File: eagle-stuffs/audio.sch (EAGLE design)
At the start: 35 parts, among them IC1 SSM2211SZ, IC2 TL084P, IC3 DS1804-100k, IC4 DS1804-10k

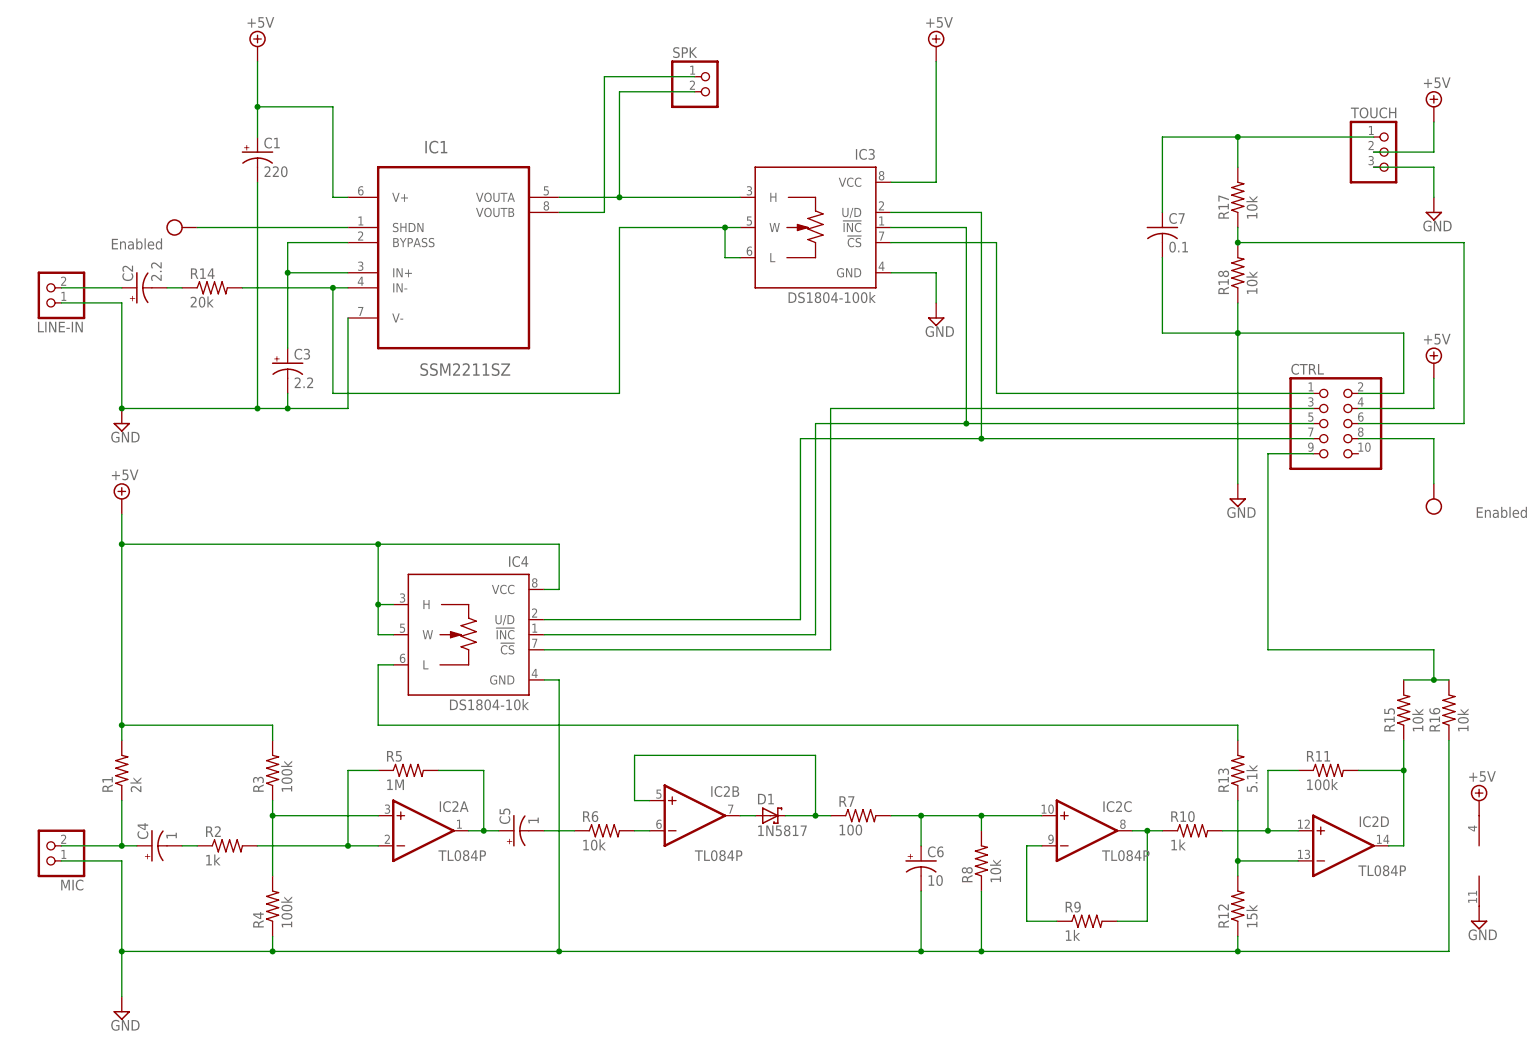
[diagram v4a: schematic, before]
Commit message: Removed second digital pot
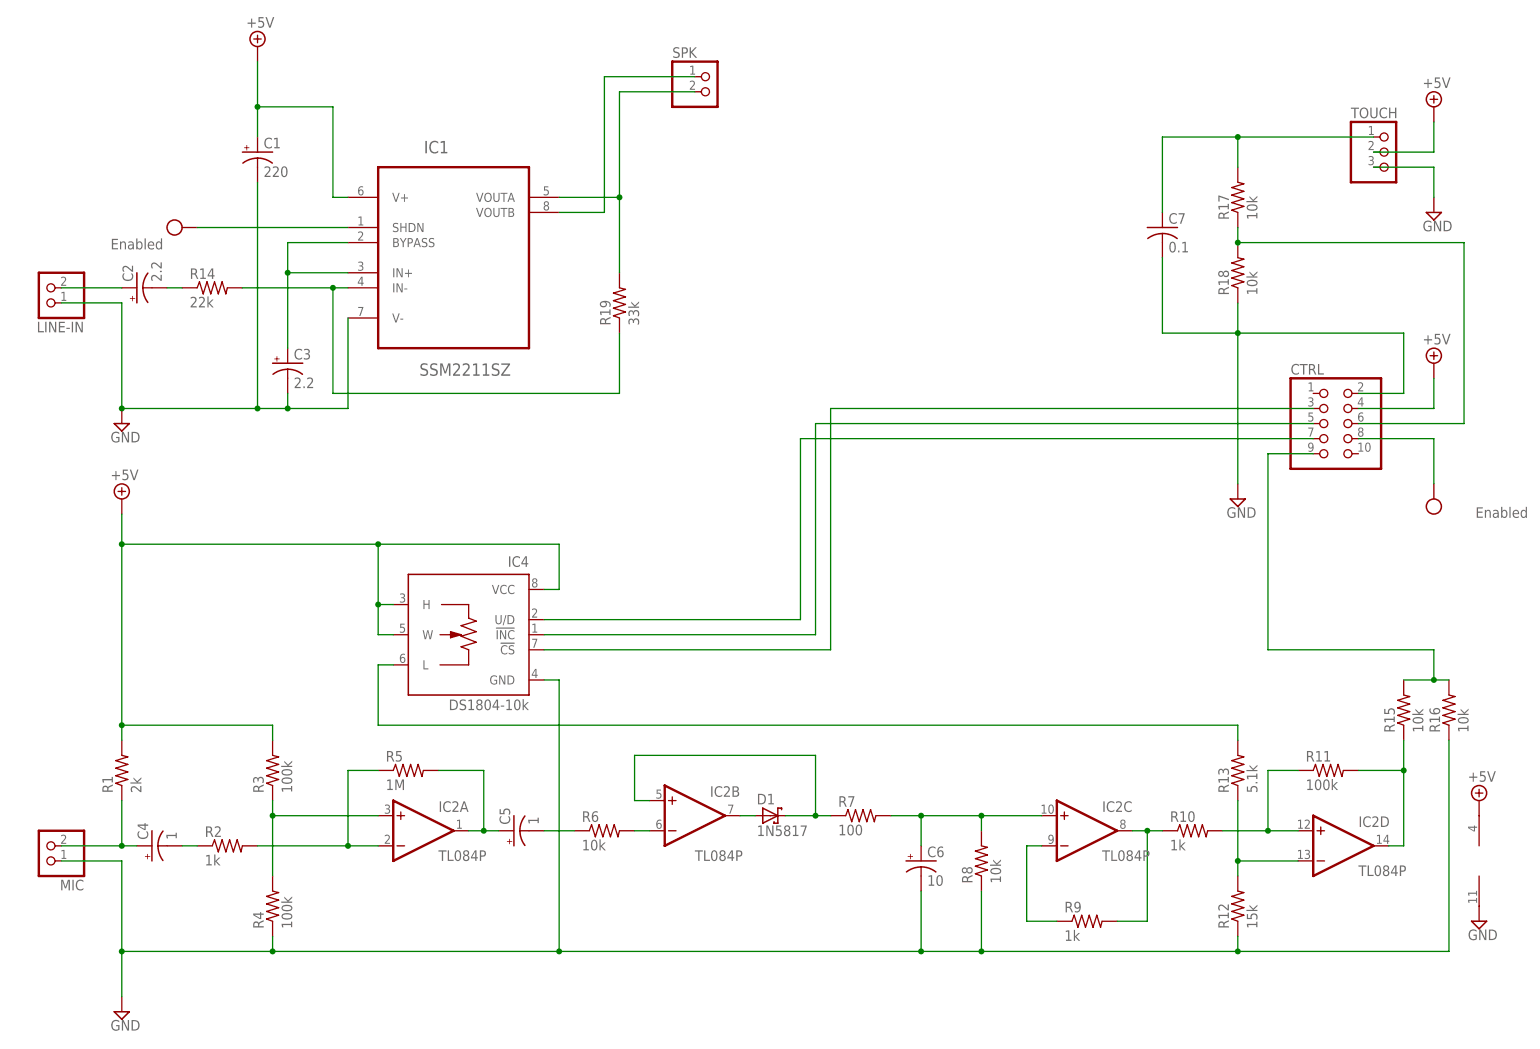
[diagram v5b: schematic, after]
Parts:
- removed IC3: DS1804-100k, pot-xicor:X9C102P
- added R19: 33k, rcl:R-US_0204/2V
- R14: value 20k -> 22k
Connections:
- removed net N$18: CTRL.1, IC3.!CS
- net +5V: no longer IC3.VCC
- net GND: no longer IC3.GND
- net N$1: now also R19.2; no longer IC3.H
- net N$20: no longer IC3.!INC
- net N$21: no longer IC3.U/D
- net N$4: now also R19.1; no longer IC3.L, IC3.W
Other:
- note added: "C"
- note removed: "B"
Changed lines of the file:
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@@
 <part name="FRAME1" library="frames" deviceset="FRAME_A_L" device=""/>
 <part name="IC2" library="linear" deviceset="TL084" device="P"/>
-<part name="IC3" library="pot-xicor" deviceset="X9C102*" device="P" value="DS1804-100k"/>
 <part name="IC4" library="pot-xicor" deviceset="X9C102*" device="P" value="DS1804-10k"/>
 <part name="SUPPLY1" library="supply2" deviceset="+5V" device=""/>
@@
 <part name="SUPPLY3" library="supply2" deviceset="VCC" device="" value="Enabled"/>
 <part name="SUPPLY6" library="supply2" deviceset="VCC" device="" value="Enabled"/>
-<part name="SUPPLY9" library="supply2" deviceset="+5V" device=""/>
-<part name="SUPPLY14" library="supply2" deviceset="GND" device=""/>
 <part name="TOUCH" library="adafruit" deviceset="PINHD-1X3" device=""/>
 <part name="SUPPLY15" library="supply2" deviceset="+5V" device=""/>
@@
 <part name="D1" library="adafruit" deviceset="SCHOTTKY-DIODE" device="DO41-7" value="1N5817"/>
 <part name="C6" library="rcl" deviceset="CPOL-US" device="E2-4" value="10"/>
-<part name="R14" library="rcl" deviceset="R-US_" device="0204/2V" value="20k"/>
+<part name="R14" library="rcl" deviceset="R-US_" device="0204/2V" value="22k"/>
 <part name="R2" library="rcl" deviceset="R-US_" device="0204/2V" value="1k"/>
 <part name="R5" library="rcl" deviceset="R-US_" device="0204/2V" value="1M"/>
@@
 <part name="R18" library="rcl" deviceset="R-US_" device="0204/2V" value="10k"/>
 <part name="C7" library="rcl" deviceset="C-US" device="025-024X044" value="0.1"/>
+<part name="R19" library="rcl" deviceset="R-US_" device="0204/2V" value="33k"/>
 </parts>
 <sheets>
@@
 <text x="193.04" y="25.4" size="2.54" layer="98" font="fixed">Y.A.N.C. (Yet Another Nixie Clock)</text>
 <text x="175.26" y="7.62" size="2.54" layer="98" font="fixed">Licensed under CERN OHL v.1.2 or later</text>
-<text x="264.16" y="7.62" size="2.54" layer="98" font="fixed">B</text>
+<text x="264.16" y="7.62" size="2.54" layer="98" font="fixed">C</text>
 <text x="76.2" y="45.72" size="1.778" layer="98" font="fixed">Preamp</text>
 <text x="132.08" y="45.72" size="1.778" layer="98" font="fixed">Envelope follower</text>
@@
 <attribute name="VALUE" x="129.54" y="66.04" size="1.778" layer="96"/>
 </instance>
-<instance part="IC3" gate="1" x="149.86" y="172.72" rot="MR0"/>
 <instance part="IC4" gate="1" x="91.44" y="104.14" rot="MR0"/>
 <instance part="SUPPLY1" gate="+5V" x="254" y="149.86"/>
@@
 <attribute name="VALUE" x="269.875" y="123.825" size="1.778" layer="96" rot="MR0"/>
 </instance>
-<instance part="SUPPLY9" gate="+5V" x="170.18" y="203.2" smashed="yes">
-<attribute name="VALUE" x="168.275" y="206.375" size="1.778" layer="96"/>
-</instance>
-<instance part="SUPPLY14" gate="GND" x="170.18" y="157.48"/>
 <instance part="TOUCH" gate="A" x="246.38" y="185.42"/>
 <instance part="SUPPLY15" gate="+5V" x="254" y="193.04"/>
@@
 <instance part="R18" gate="G$1" x="220.98" y="165.1" rot="R90"/>
 <instance part="C7" gate="G$1" x="208.28" y="172.72"/>
+<instance part="R19" gate="G$1" x="116.84" y="160.02" rot="R90"/>
 </instances>
 <busses>
@@
 </segment>
 <segment>
-<pinref part="IC3" gate="1" pin="GND"/>
-<pinref part="SUPPLY14" gate="GND" pin="GND"/>
-<wire x1="162.56" y1="165.1" x2="170.18" y2="165.1" width="0.1524" layer="91"/>
-<wire x1="170.18" y1="165.1" x2="170.18" y2="160.02" width="0.1524" layer="91"/>
-</segment>
-<segment>
 <pinref part="TOUCH" gate="A" pin="3"/>
 <wire x1="243.84" y1="182.88" x2="254" y2="182.88" width="0.1524" layer="91"/>
@@
 </segment>
 <segment>
-<pinref part="IC3" gate="1" pin="VCC"/>
-<pinref part="SUPPLY9" gate="+5V" pin="+5V"/>
-<wire x1="162.56" y1="180.34" x2="170.18" y2="180.34" width="0.1524" layer="91"/>
-<wire x1="170.18" y1="180.34" x2="170.18" y2="200.66" width="0.1524" layer="91"/>
-</segment>
-<segment>
 <pinref part="TOUCH" gate="A" pin="2"/>
 <pinref part="SUPPLY15" gate="+5V" pin="+5V"/>
@@
 <segment>
 <pinref part="IC4" gate="1" pin="!INC"/>
-<wire x1="149.86" y1="139.7" x2="175.26" y2="139.7" width="0.1524" layer="91"/>
-<wire x1="175.26" y1="139.7" x2="233.68" y2="139.7" width="0.1524" layer="91"/>
+<wire x1="149.86" y1="139.7" x2="233.68" y2="139.7" width="0.1524" layer="91"/>
 <wire x1="104.14" y1="104.14" x2="149.86" y2="104.14" width="0.1524" layer="91"/>
 <wire x1="149.86" y1="104.14" x2="149.86" y2="139.7" width="0.1524" layer="91"/>
 <pinref part="CTRL" gate="A" pin="5"/>
-<pinref part="IC3" gate="1" pin="!INC"/>
-<wire x1="162.56" y1="172.72" x2="175.26" y2="172.72" width="0.1524" layer="91"/>
-<wire x1="175.26" y1="172.72" x2="175.26" y2="139.7" width="0.1524" layer="91"/>
-<junction x="175.26" y="139.7"/>
 </segment>
 </net>
@@
 <segment>
 <pinref part="IC4" gate="1" pin="U/D"/>
-<wire x1="147.32" y1="137.16" x2="177.8" y2="137.16" width="0.1524" layer="91"/>
-<wire x1="177.8" y1="137.16" x2="233.68" y2="137.16" width="0.1524" layer="91"/>
+<wire x1="147.32" y1="137.16" x2="233.68" y2="137.16" width="0.1524" layer="91"/>
 <wire x1="104.14" y1="106.68" x2="147.32" y2="106.68" width="0.1524" layer="91"/>
 <wire x1="147.32" y1="106.68" x2="147.32" y2="137.16" width="0.1524" layer="91"/>
 <pinref part="CTRL" gate="A" pin="7"/>
-<pinref part="IC3" gate="1" pin="U/D"/>
-<wire x1="162.56" y1="175.26" x2="177.8" y2="175.26" width="0.1524" layer="91"/>
-<wire x1="177.8" y1="175.26" x2="177.8" y2="137.16" width="0.1524" layer="91"/>
-<junction x="177.8" y="137.16"/>
 </segment>
 </net>
@@
 <wire x1="68.58" y1="162.56" x2="68.58" y2="144.78" width="0.1524" layer="91"/>
 <wire x1="68.58" y1="144.78" x2="116.84" y2="144.78" width="0.1524" layer="91"/>
-<wire x1="116.84" y1="144.78" x2="116.84" y2="172.72" width="0.1524" layer="91"/>
 <junction x="68.58" y="162.56"/>
-<pinref part="IC3" gate="1" pin="W"/>
-<wire x1="137.16" y1="172.72" x2="134.62" y2="172.72" width="0.1524" layer="91"/>
-<wire x1="116.84" y1="172.72" x2="134.62" y2="172.72" width="0.1524" layer="91"/>
-<pinref part="IC3" gate="1" pin="L"/>
-<wire x1="137.16" y1="167.64" x2="134.62" y2="167.64" width="0.1524" layer="91"/>
-<wire x1="134.62" y1="167.64" x2="134.62" y2="172.72" width="0.1524" layer="91"/>
-<junction x="134.62" y="172.72"/>
 <pinref part="R14" gate="G$1" pin="2"/>
+<pinref part="R19" gate="G$1" pin="1"/>
+<wire x1="116.84" y1="144.78" x2="116.84" y2="154.94" width="0.1524" layer="91"/>
 </segment>
 </net>
@@
 <pinref part="IC1" gate="A" pin="VOUTA"/>
 <wire x1="116.84" y1="177.8" x2="106.68" y2="177.8" width="0.1524" layer="91"/>
-<pinref part="IC3" gate="1" pin="H"/>
-<wire x1="116.84" y1="177.8" x2="137.16" y2="177.8" width="0.1524" layer="91"/>
+<pinref part="R19" gate="G$1" pin="2"/>
+<wire x1="116.84" y1="165.1" x2="116.84" y2="177.8" width="0.1524" layer="91"/>
 <junction x="116.84" y="177.8"/>
 </segment>
@@
 </segment>
 </net>
-<net name="N$18" class="0">
-<segment>
-<pinref part="CTRL" gate="A" pin="1"/>
-<wire x1="233.68" y1="144.78" x2="180.34" y2="144.78" width="0.1524" layer="91"/>
-<wire x1="180.34" y1="144.78" x2="180.34" y2="170.18" width="0.1524" layer="91"/>
-<pinref part="IC3" gate="1" pin="!CS"/>
-<wire x1="180.34" y1="170.18" x2="162.56" y2="170.18" width="0.1524" layer="91"/>
-</segment>
-</net>
